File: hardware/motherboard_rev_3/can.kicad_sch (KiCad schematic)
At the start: 9 parts, among them J5 Conn_01x04, J6 Conn_01x04, U13 TCAN3403

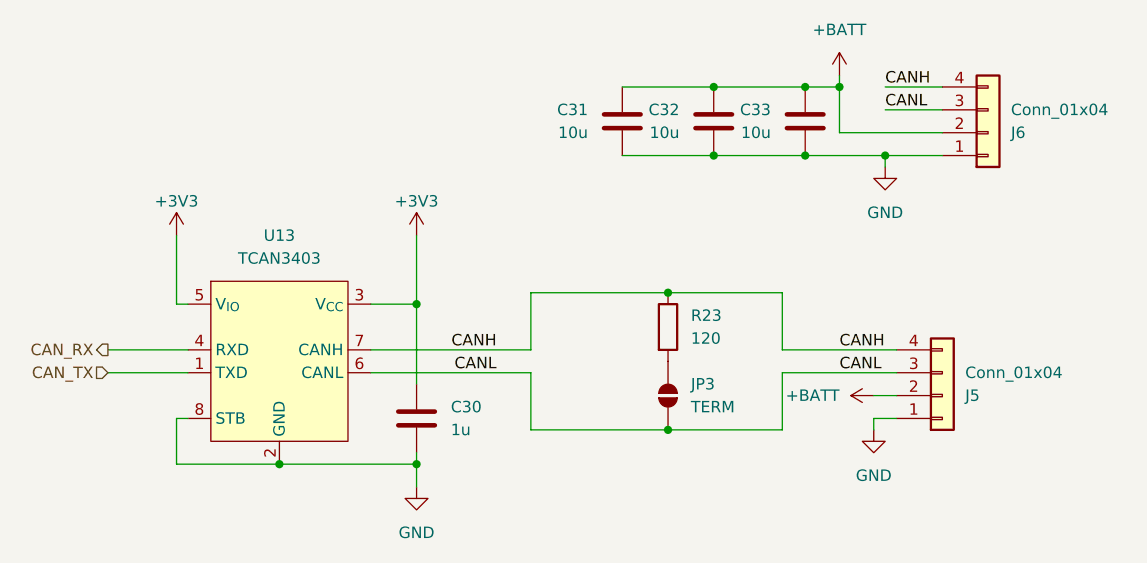
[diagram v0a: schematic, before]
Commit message: Completed schematic for rev 3.0 PCB
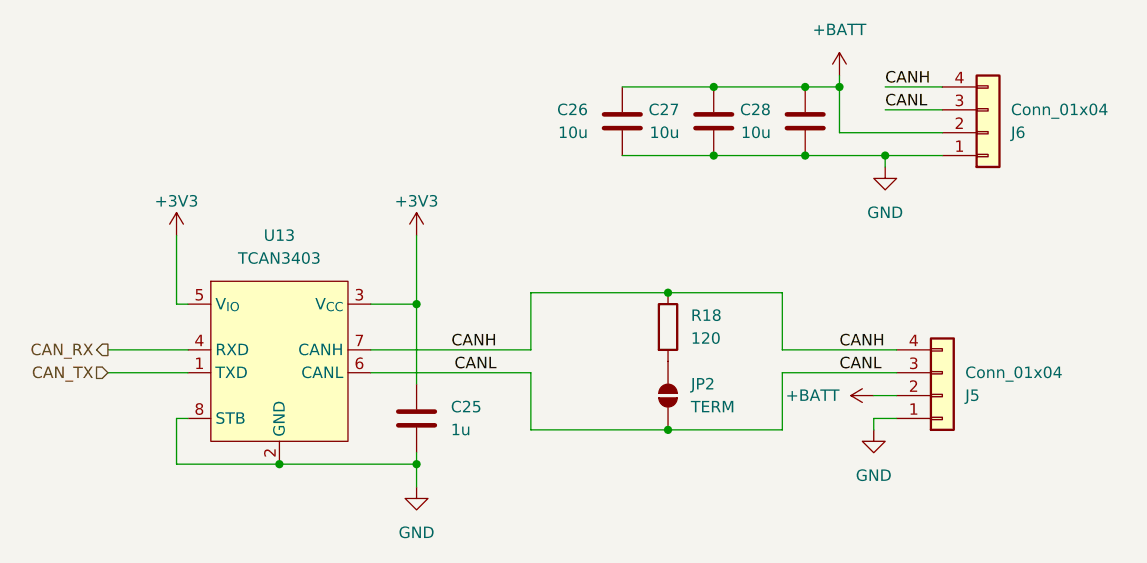
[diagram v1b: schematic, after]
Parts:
- renumbered C30 to C25, C31 to C26, C32 to C27, C33 to C28, JP3 to JP2, R23 to R18
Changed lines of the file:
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@@
 		(dnp no)
 		(fields_autoplaced yes)
-		(property "Reference" "#PWR060"
+		(property "Reference" "#PWR054"
 			(at 186.69 110.49 0)
 			(effects
@@
 			(project "wing_module_rev_1"
 				(path "/39c7ec0f-0a05-4172-b48a-dcc9b63f77ff/7b980629-eac8-442c-9575-c3552746993e"
-					(reference "#PWR060")
+					(reference "#PWR054")
 					(unit 1)
 				)
@@
 		(on_board yes)
 		(dnp no)
-		(property "Reference" "C31"
+		(property "Reference" "C26"
 			(at 151.13 78.7399 0)
 			(effects
@@
 			(project "wing_module_rev_1"
 				(path "/39c7ec0f-0a05-4172-b48a-dcc9b63f77ff/7b980629-eac8-442c-9575-c3552746993e"
-					(reference "C31")
+					(reference "C26")
 					(unit 1)
 				)
@@
 		(on_board yes)
 		(dnp no)
-		(property "Reference" "C33"
+		(property "Reference" "C28"
 			(at 171.45 78.7399 0)
 			(effects
@@
 			(project "wing_module_rev_1"
 				(path "/39c7ec0f-0a05-4172-b48a-dcc9b63f77ff/7b980629-eac8-442c-9575-c3552746993e"
-					(reference "C33")
+					(reference "C28")
 					(unit 1)
 				)
@@
 		(on_board yes)
 		(dnp no)
-		(property "Reference" "C32"
+		(property "Reference" "C27"
 			(at 161.29 78.7399 0)
 			(effects
@@
 			(project "wing_module_rev_1"
 				(path "/39c7ec0f-0a05-4172-b48a-dcc9b63f77ff/7b980629-eac8-442c-9575-c3552746993e"
-					(reference "C32")
+					(reference "C27")
 					(unit 1)
 				)
@@
 		(dnp no)
 		(fields_autoplaced yes)
-		(property "Reference" "C30"
+		(property "Reference" "C25"
 			(at 135.89 111.7599 0)
 			(effects
@@
 			(project "wing_module_rev_1"
 				(path "/39c7ec0f-0a05-4172-b48a-dcc9b63f77ff/7b980629-eac8-442c-9575-c3552746993e"
-					(reference "C30")
+					(reference "C25")
 					(unit 1)
 				)
@@
 		(dnp no)
 		(fields_autoplaced yes)
-		(property "Reference" "JP3"
+		(property "Reference" "JP2"
 			(at 162.56 109.2199 90)
 			(effects
@@
 			(project "wing_module_rev_1"
 				(path "/39c7ec0f-0a05-4172-b48a-dcc9b63f77ff/7b980629-eac8-442c-9575-c3552746993e"
-					(reference "JP3")
+					(reference "JP2")
 					(unit 1)
 				)
@@
 		(dnp no)
 		(fields_autoplaced yes)
-		(property "Reference" "#PWR058"
+		(property "Reference" "#PWR052"
 			(at 132.08 127 0)
 			(effects
@@
 			(project "wing_module_rev_1"
 				(path "/39c7ec0f-0a05-4172-b48a-dcc9b63f77ff/7b980629-eac8-442c-9575-c3552746993e"
-					(reference "#PWR058")
+					(reference "#PWR052")
 					(unit 1)
 				)
@@
 		(on_board yes)
 		(dnp no)
-		(property "Reference" "#PWR056"
+		(property "Reference" "#PWR050"
 			(at 105.41 96.52 0)
 			(effects
@@
 			(project "wing_module_rev_1"
 				(path "/39c7ec0f-0a05-4172-b48a-dcc9b63f77ff/7b980629-eac8-442c-9575-c3552746993e"
-					(reference "#PWR056")
+					(reference "#PWR050")
 					(unit 1)
 				)
@@
 		(dnp no)
 		(fields_autoplaced yes)
-		(property "Reference" "R23"
+		(property "Reference" "R18"
 			(at 162.56 101.5999 0)
 			(effects
@@
 			(project "wing_module_rev_1"
 				(path "/39c7ec0f-0a05-4172-b48a-dcc9b63f77ff/7b980629-eac8-442c-9575-c3552746993e"
-					(reference "R23")
+					(reference "R18")
 					(unit 1)
 				)
@@
 		(dnp no)
 		(fields_autoplaced yes)
-		(property "Reference" "#PWR061"
+		(property "Reference" "#PWR055"
 			(at 182.88 120.65 0)
 			(effects
@@
 			(project "wing_module_rev_1"
 				(path "/39c7ec0f-0a05-4172-b48a-dcc9b63f77ff/7b980629-eac8-442c-9575-c3552746993e"
-					(reference "#PWR061")
+					(reference "#PWR055")
 					(unit 1)
 				)
@@
 		(on_board yes)
 		(dnp no)
-		(property "Reference" "#PWR057"
+		(property "Reference" "#PWR051"
 			(at 132.08 96.52 0)
 			(effects
@@
 			(project "wing_module_rev_1"
 				(path "/39c7ec0f-0a05-4172-b48a-dcc9b63f77ff/7b980629-eac8-442c-9575-c3552746993e"
-					(reference "#PWR057")
+					(reference "#PWR051")
 					(unit 1)
 				)
@@
 		(dnp no)
 		(fields_autoplaced yes)
-		(property "Reference" "#PWR059"
+		(property "Reference" "#PWR053"
 			(at 179.07 78.74 0)
 			(effects
@@
 			(project "wing_module_rev_1"
 				(path "/39c7ec0f-0a05-4172-b48a-dcc9b63f77ff/7b980629-eac8-442c-9575-c3552746993e"
-					(reference "#PWR059")
+					(reference "#PWR053")
 					(unit 1)
 				)
@@
 		(dnp no)
 		(fields_autoplaced yes)
-		(property "Reference" "#PWR062"
+		(property "Reference" "#PWR056"
 			(at 184.15 91.44 0)
 			(effects
@@
 			(project "wing_module_rev_1"
 				(path "/39c7ec0f-0a05-4172-b48a-dcc9b63f77ff/7b980629-eac8-442c-9575-c3552746993e"
-					(reference "#PWR062")
-					(unit 1)
-				)
+					(reference "#PWR056")
+					(unit 1)
+				)

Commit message: Removed LDO and just regulate to 3.3V, also removed off board CO2
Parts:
- removed C26: 10u, Capacitor_SMD:C_0603_1608Metric, symbol Device:C
- removed JP2: TERM, Jumper:SolderJumper-2_P1.3mm_Open_TrianglePad1.0x1.5mm, symbol Jumper:SolderJumper_2_Open
- removed R18: 120, Resistor_SMD:R_0402_1005Metric, symbol Device:R
- added C23, C25: 10u, Capacitor_SMD:C_0603_1608Metric, symbol Device:C
- J5: renamed from J6; value Conn_01x04 -> EH_S4B-EH; footprint Connector_JST:JST_EH_B4B-EH-A_1x04_P2.50mm_Vertical -> Connector_JST:JST_EH_S4B-EH_1x04_P2.50mm_Horizontal; LCSC C160258 -> C265068
- J6: renamed from J5; value Conn_01x04 -> EH_S4B-EH; footprint Connector_JST:JST_EH_B4B-EH-A_1x04_P2.50mm_Vertical -> Connector_JST:JST_EH_S4B-EH_1x04_P2.50mm_Horizontal; LCSC C160258 -> C265068
- renumbered C25 to C21, C27 to C22, C28 to C24
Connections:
- net GND: now also C23.2, C25.2
- net +BATT renamed +12V
- net +12V: now also C23.1, C25.1
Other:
- moved on the sheet: C22, C24, J5
